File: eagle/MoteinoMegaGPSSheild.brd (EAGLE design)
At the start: 100 x 80 mm, 10 parts, among them Q2 NDP6020P P-CHANNEL

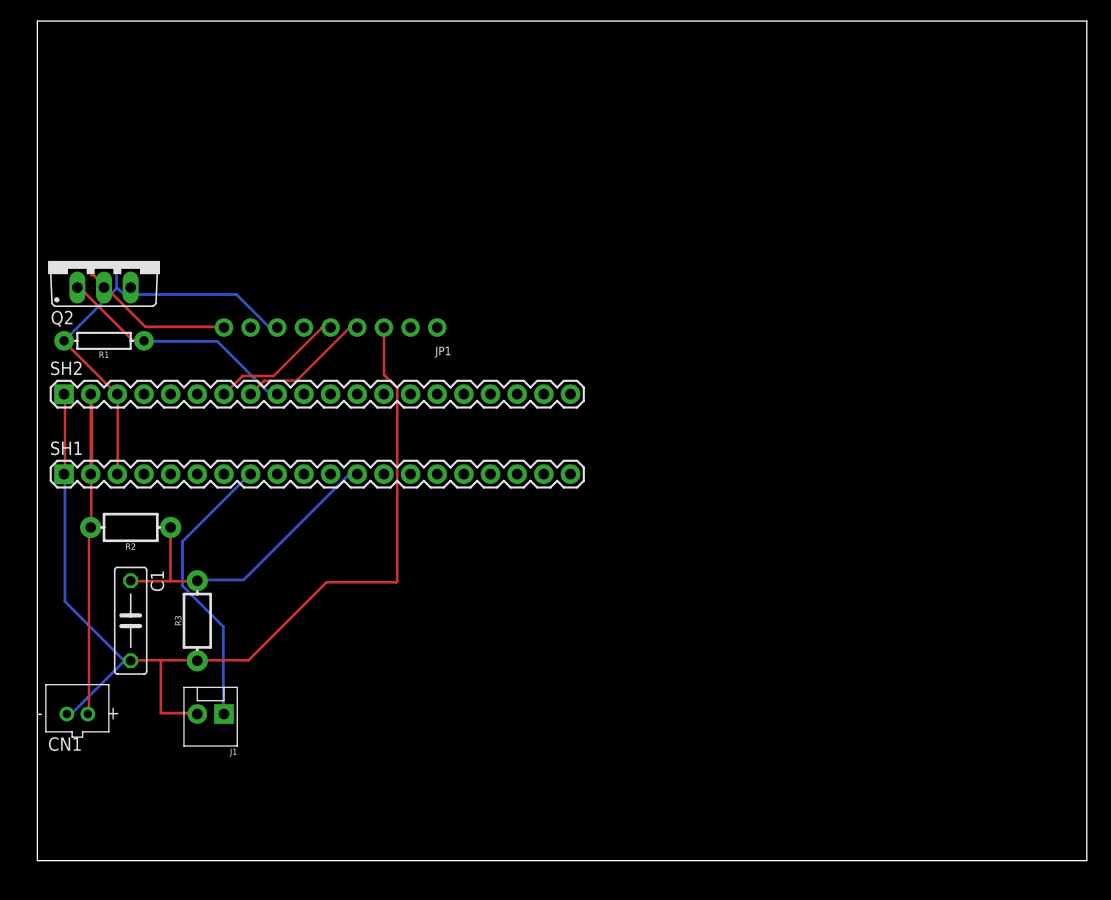
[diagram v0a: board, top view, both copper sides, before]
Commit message: V0.2 No errors, Bottom layer copper pour
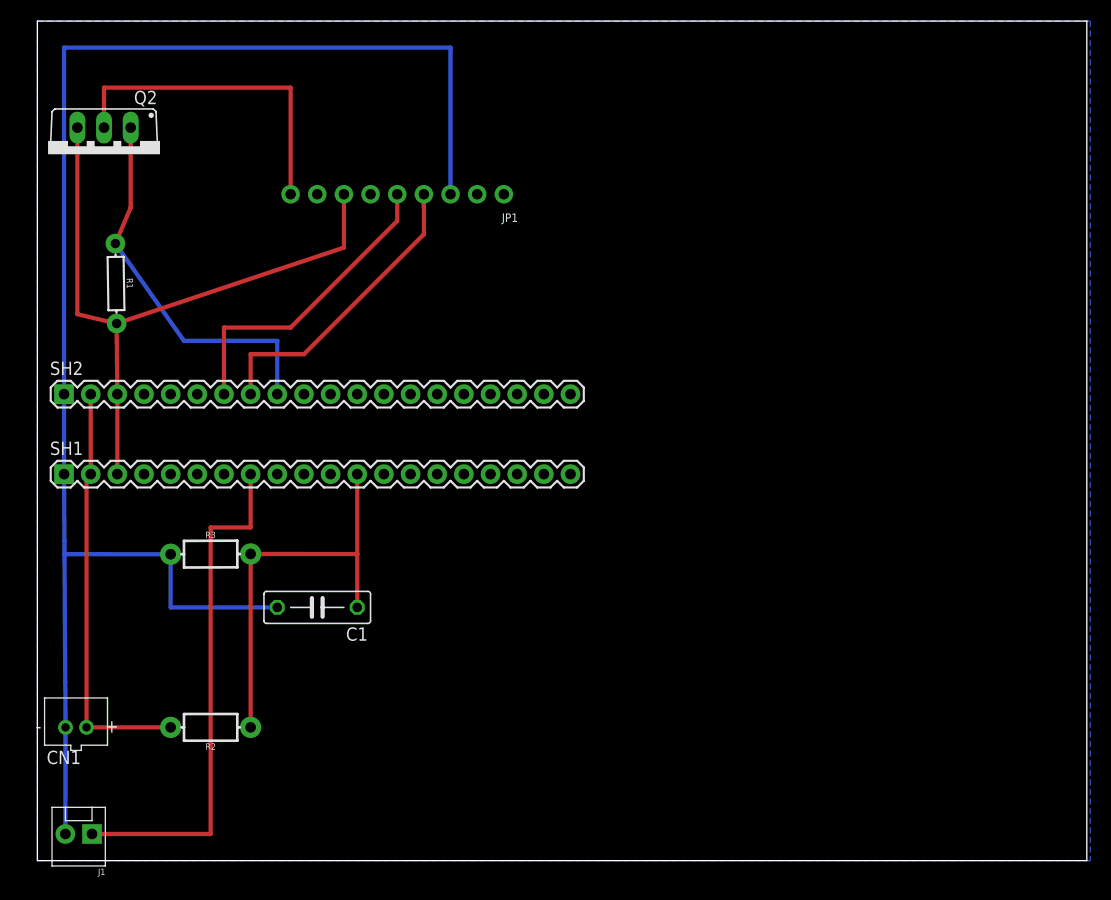
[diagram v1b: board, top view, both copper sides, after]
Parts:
- CN1: value (none) -> JST
- J1: value (none) -> SCREW_TERM
- JP1: value (none) -> GPS_HEADR
- moved R2 20.5 mm to (16.5, 12.7)
- moved C1 17.8 mm to (26.7, 24.1), turned to 180 degrees
- moved J1 17.0 mm to (5.21, 2.54)
- moved JP1 14.2 mm to (34.3, 63.5)
- moved Q2 10.2 mm to (6.35, 67.3), turned to 180 degrees
- moved R3 6.48 mm to (16.5, 29.2), turned to 0.2 degrees
- moved R1 5.58 mm to (7.49, 55.0), turned to 270.9 degrees
- moved CN1 1.28 mm to (3.68, 12.7)
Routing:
- net GND: track 98.5 -> 151.1 mm
- net VBAT: track 40.8 -> 63.9 mm
- net D3: track 27.2 -> 49.4 mm
- net D11_TX1: track 12.8 -> 30.1 mm
- net 3.3V: track 14.8 -> 31.8 mm
- net D10_RX1: track 12.8 -> 29.6 mm
- net D12: track 23.3 -> 36.7 mm
- net PWR: track 30.9 -> 39.9 mm
- net A0: track 30.9 -> 39.4 mm
- added copper zone on layer 16, net GND

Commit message: v0.3 ... GSM plus right Mega headers
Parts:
- removed SH1, SH2: M20, SparkFun-Connectors:1X20
- added FONA_GSM: HEADER, adafruit2:1X12-CB
- added J2, J3, J4, J5, J6: SCREW_TERM, SparkFun-Connectors:SCREWTERMINAL-3.5MM-2-NS
- added U$1: MOTEINO_MEGA_SIMPLE, Moteino:MOTEINO_MEGA_SIMPLE
- C1: value 0.01uF -> 0.1uF
- J1: device SparkFun-Retired:MOLEX-1X2 -> SparkFun-Connectors:SCREWTERMINAL-3.5MM-2-NS
- moved JP1 9.25 mm to (31.8, 72.4)
- moved Q2 8.89 mm to (6.35, 76.2), turned to 0 degrees
- moved R3 7.62 mm to (16.5, 21.6), turned to 0 degrees
- moved R1 7.24 mm to (7.62, 62.2), turned to 0 degrees
- moved C1 6.84 mm to (24.1, 17.8), turned to 0 degrees
- moved CN1 5.08 mm to (3.81, 17.8)
- moved J1 2.95 mm to (2.54, 3.81), turned to 0 degrees
- moved R2 1.27 mm to (16.5, 14.0)
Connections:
- removed net A5: SH1.17
- removed net A6: SH1.18
- removed net A7: SH1.19
- removed net AREF: SH1.20
- removed net D0: SH1.11
- removed net D13: SH2.10
- removed net D14: SH2.11
- removed net D15: SH2.12
- removed net D16: SH2.13
- removed net D17: SH2.14
- removed net D18: SH2.15
- removed net D19: SH2.16
- removed net D2: SH1.9
- removed net D20: SH2.17
- removed net D21: SH2.18
- removed net D22: SH2.19
- removed net D23: SH2.20
- removed net D4_SS: SH1.7
- removed net D5_MOSI: SH1.6
- removed net D6_MISO: SH1.5
- removed net D7_SCK: SH1.4
- removed net PWR: CN1.1, R2.P$2, SH1.2, SH2.2
- removed net RST: SH2.4
- removed net VBAT: JP1.7, Q2.S, R1.P$2, SH1.3, SH2.3
- new net D13_NETSTAT: FONA_GSM.2, U$1.D13
- new net D14_KEY: FONA_GSM.6, U$1.D14
- new net D18_PS: FONA_GSM.7, U$1.D18
- new net N$3: J6.2
- new net SPEAKER2+: FONA_GSM.10
- new net VIN: CN1.1, FONA_GSM.12, R2.P$2, U$1.VIN
- net 3.3V: now also FONA_GSM.1, JP1.7, Q2.S, R1.P$2, U$1.3V3_2
- net A0: now also U$1.A0; no longer SH1.12
- net A1: now also U$1.A1; no longer SH1.13
- net A2: now also J2.2, J3.2, U$1.A2; no longer SH1.14
- net A3: now also J5.2, U$1.A3; no longer SH1.15
- net A4: now also J6.1, U$1.A4; no longer SH1.16
- net D1: now also J4.2, U$1.D1; no longer SH1.10
- net D10_RX1: now also U$1.D10; no longer SH2.7
- net D11_TX1: now also U$1.D11; no longer SH2.8
- net D12: now also U$1.D12; no longer SH2.9
- net D3: now also J1.2, U$1.D3; no longer J1.1, SH1.8
- net D8: now also FONA_GSM.4, U$1.D8; no longer SH2.5
- net D9: now also FONA_GSM.3, U$1.D9; no longer SH2.6
- net GND: now also FONA_GSM.11, J1.1, J2.1, J3.1, J4.1, J5.1, U$1.GND1, U$1.GND_2; no longer J1.2, SH1.1, SH2.1
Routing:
- net GND: track 151.1 -> 0.00 mm
- net 3.3V: track 31.8 -> 127.1 mm
- net VIN: track 0.00 -> 84.4 mm
- net VBAT: track 63.9 -> 0.00 mm
- net D8: track 0.00 -> 50.8 mm
- net D9: track 0.00 -> 45.7 mm
- net D14_KEY: track 0.00 -> 40.6 mm
- net PWR: track 39.9 -> 0.00 mm
- net A1: track 0.00 -> 38.0 mm
- net D1: track 0.00 -> 37.4 mm
- net A2: track 0.00 -> 34.5 mm
- net D18_PS: track 0.00 -> 33.0 mm
- net D13_NETSTAT: track 0.00 -> 33.0 mm
- net A3: track 0.00 -> 29.2 mm
- net A4: track 0.00 -> 26.5 mm
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
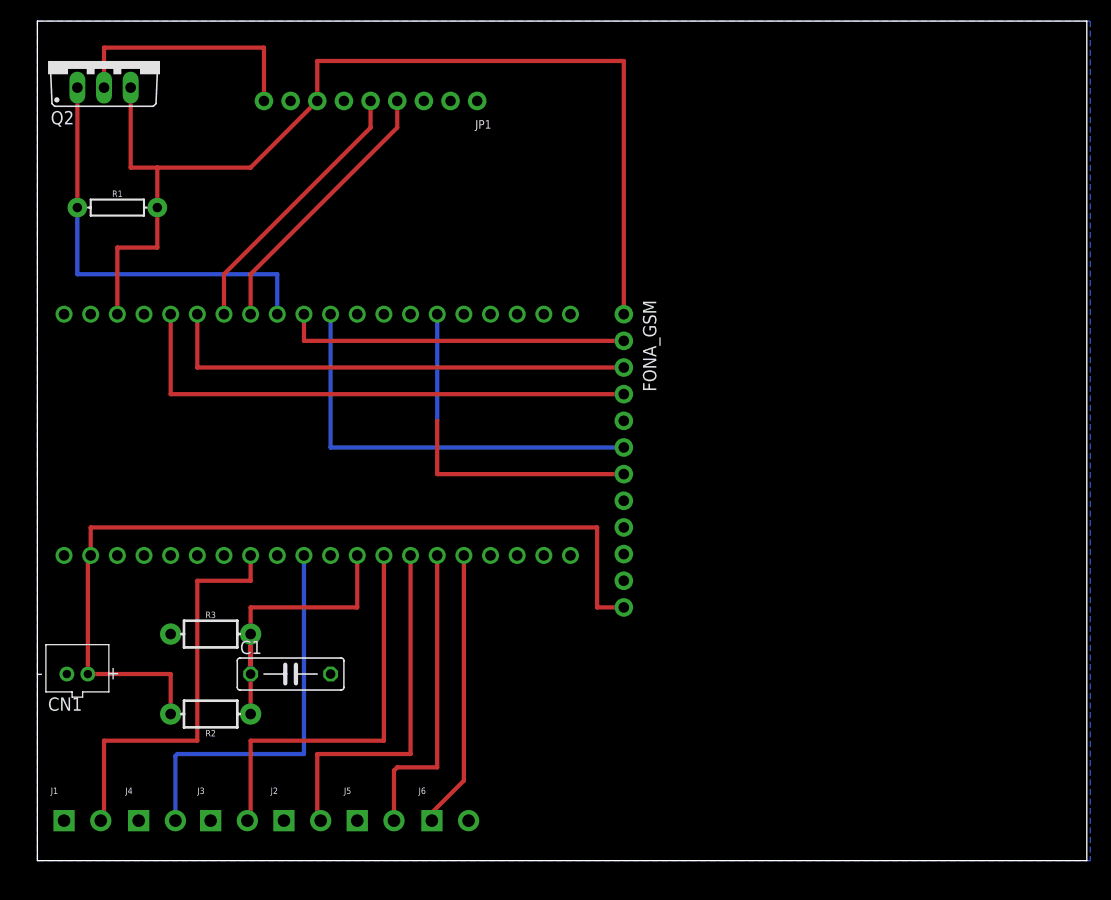
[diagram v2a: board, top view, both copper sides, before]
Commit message: Removing PDFs
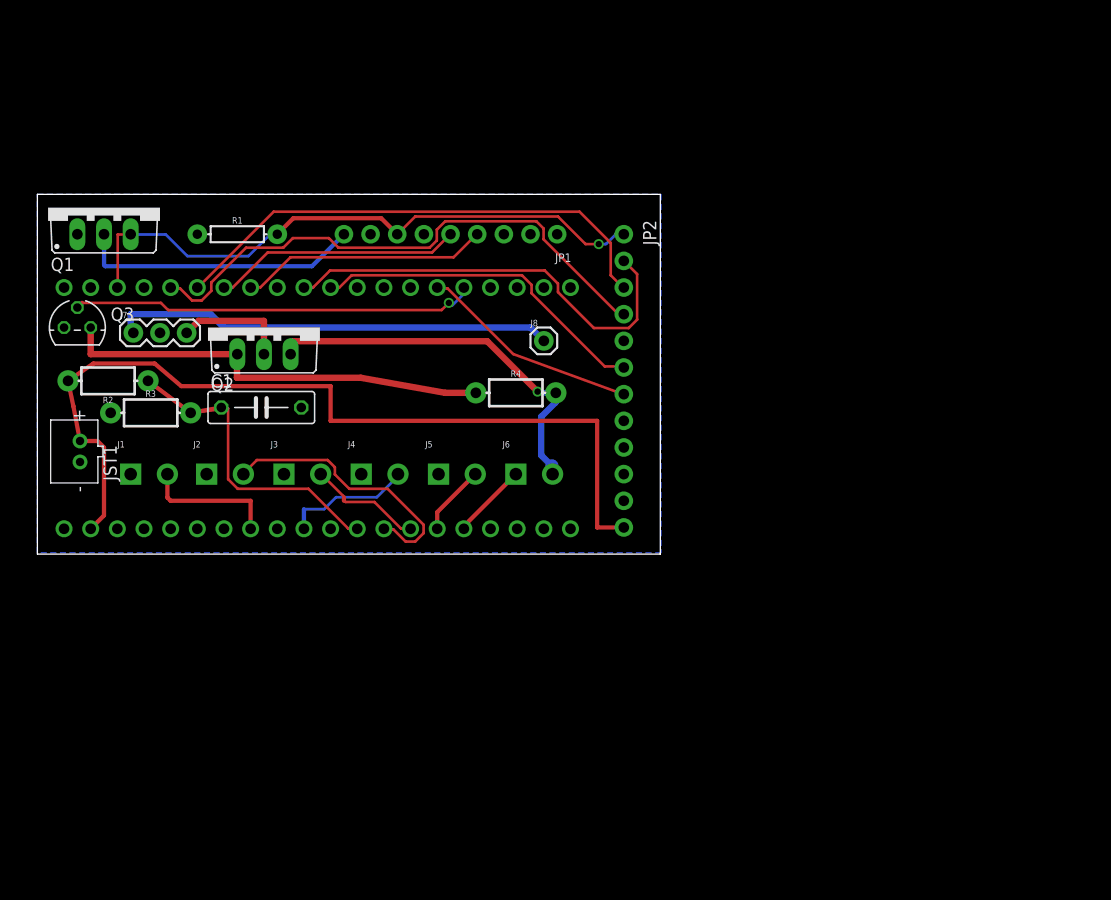
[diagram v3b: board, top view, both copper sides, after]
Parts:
- removed CN1: JST, adafruit:JST-PH-2-THM
- removed FONA_GSM: HEADER, adafruit2:1X12-CB
- removed U$1: MOTEINO_MEGA_SIMPLE, Moteino:MOTEINO_MEGA_SIMPLE
- added J7: OKI-78SR-5/1.5, SparkFun-Connectors:1X03
- added J8: 5V, SparkFun-Connectors:1X01
- added JP2: FONA_GSM, adafruit2:1X12-CB
- added JST1: LIPO, adafruit:JST-PH-2-THM
- added MOTEINO_MEGA: HEADERS, Moteino:MOTEINO_MEGA_SIMPLE
- added Q1: NDP6020P P-CHANNEL, transistor-power:TO220BV
- added Q3: 2N7000, transistors:TO-92
- added R4: 10K, SparkFun-Resistors:AXIAL-0.3-KIT
- J1: value SCREW_TERM -> BilgeSwitch
- J2: value SCREW_TERM -> Button
- J3: value SCREW_TERM -> LED
- J5: value SCREW_TERM -> DS18B20
- J6: value SCREW_TERM -> DS18B20_12-24V_VCC
- Q2: value NDP6020P P-CHANNEL -> IRF9Z14PBF
- moved J4 39.2 mm to (30.9, 36.8)
- moved J6 34.0 mm to (45.6, 36.8)
- moved J5 33.9 mm to (38.2, 36.8)
- moved J2 33.8 mm to (16.1, 36.8)
- moved J3 33.8 mm to (23.5, 36.8)
- moved J1 33.6 mm to (8.89, 36.8)
- moved R2 33.2 mm to (6.73, 45.7)
- moved Q2 29.6 mm to (21.6, 50.8)
- moved C1 25.6 mm to (21.3, 43.2)
- moved R3 21.8 mm to (10.8, 42.7)
- moved JP1 14.8 mm to (39.4, 59.7)
- moved R1 11.7 mm to (19.1, 59.7)
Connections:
- removed net A1: U$1.A1
- removed net A2: J2.2, J3.2, U$1.A2
- removed net A3: J5.2, U$1.A3
- removed net A4: J6.1, U$1.A4
- removed net N$3: J6.2
- new net 12-24V-SW: J7.3, Q2.D
- new net 12-24V-VCC: J6.2, Q2.S, R4.P$2
- new net 5V_VCC: J7.1, J8.1
- new net D19_PWRON: MOTEINO_MEGA.D19, Q3.2
- new net D25: J2.2, MOTEINO_MEGA.A1
- new net D26: J3.2, MOTEINO_MEGA.A2
- new net D27: J5.2, MOTEINO_MEGA.A3
- new net D28: J6.1, MOTEINO_MEGA.A4
- new net GPS_VCC: JP1.9, Q1.D
- new net N$2: Q2.G, Q3.3, R4.P$1
- net 3.3V: now also JP2.1, MOTEINO_MEGA.3V3_2, Q1.S; no longer FONA_GSM.1, JP1.9, Q2.D, Q2.S, U$1.3V3_2
- net A0: now also MOTEINO_MEGA.A0; no longer U$1.A0
- net D1: now also MOTEINO_MEGA.D1; no longer U$1.D1
- net D10_RX1: now also MOTEINO_MEGA.D10; no longer U$1.D10
- net D11_TX1: now also MOTEINO_MEGA.D11; no longer U$1.D11
- net D12: now also MOTEINO_MEGA.D12, Q1.G; no longer Q2.G, U$1.D12
- net D13_NETSTAT: now also JP2.2, MOTEINO_MEGA.D13; no longer FONA_GSM.2, U$1.D13
- net D14_KEY: now also JP2.6, MOTEINO_MEGA.D14; no longer FONA_GSM.6, U$1.D14
- net D18_PS: now also JP2.7, MOTEINO_MEGA.D18; no longer FONA_GSM.7, U$1.D18
- net D3: now also MOTEINO_MEGA.D3; no longer U$1.D3
- net D8: now also JP2.4, MOTEINO_MEGA.D8; no longer FONA_GSM.4, U$1.D8
- net D9: now also JP2.3, MOTEINO_MEGA.D9; no longer FONA_GSM.3, U$1.D9
- net GND: now also J7.2, JP2.11, JST1.2, MOTEINO_MEGA.GND1, MOTEINO_MEGA.GND_2, Q3.1; no longer CN1.2, FONA_GSM.11, U$1.GND1, U$1.GND_2
- net SPEAKER2+: now also JP2.10; no longer FONA_GSM.10
- net VIN: now also JP2.12, JST1.1, MOTEINO_MEGA.VIN; no longer CN1.1, FONA_GSM.12, U$1.VIN
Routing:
- net 3.3V: track 127.1 -> 58.4 mm, vias 0 -> 1
- net 5V_VCC: track 0.00 -> 42.3 mm
- net N$2: track 0.00 -> 41.7 mm
- net D12: track 40.6 -> 0.00 mm
- net D19_PWRON: track 0.00 -> 38.7 mm, vias 0 -> 1
- net A1: track 38.0 -> 0.00 mm
- net 12-24V-VCC: track 0.00 -> 37.2 mm, vias 0 -> 1
- net A2: track 34.5 -> 0.00 mm
- net A3: track 29.2 -> 0.00 mm
- net GPS_VCC: track 0.00 -> 27.1 mm
- net D3: track 39.6 -> 13.0 mm
- net A4: track 26.5 -> 0.00 mm
- net D25: track 0.00 -> 26.2 mm
- net D1: track 37.4 -> 12.3 mm
- net D18_PS: track 33.0 -> 21.1 mm
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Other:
- board size 100 x 80 mm -> 59.4 x 34.3 mm

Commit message: fixes....
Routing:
- net D12: track 0.00 -> 35.5 mm
- net 3.3V: track 58.4 -> 57.8 mm
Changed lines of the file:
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@@
 <attribute name="PROD_ID" value="RES-09559" x="45.593" y="44.577" size="1.778" layer="27" display="off"/>
 </element>
-<element name="Q3" library="transistors" package="TO-92" value="2N7000" x="3.81" y="50.8"/>
+<element name="Q3" library="transistors" package="TO-92" value="2N7000" x="3.81" y="50.8" smashed="yes">
+<attribute name="NAME" x="6.985" y="51.435" size="1.27" layer="25" ratio="10"/>
+<attribute name="VALUE" x="1.143" y="47.752" size="1.27" layer="27" ratio="10"/>
+</element>
 <element name="J7" library="SparkFun-Connectors" package="1X03" value="OKI-78SR-5/1.5" x="9.144" y="50.292">
 <attribute name="PROD_ID" value="XXX-00000" x="9.144" y="50.292" size="1.778" layer="27" display="off"/>
@@
 <contactref element="R1" pad="P$1"/>
 <contactref element="Q1" pad="G"/>
-<wire x1="15.24" y1="59.69" x2="22.86" y2="54.61" width="0" layer="19" extent="1-1"/>
-<wire x1="3.81" y1="59.69" x2="15.24" y2="59.69" width="0" layer="19" extent="1-1"/>
+<wire x1="3.81" y1="59.69" x2="3.81" y2="62.23" width="0.6096" layer="1"/>
+<wire x1="3.81" y1="62.23" x2="11.43" y2="62.23" width="0.6096" layer="1"/>
+<wire x1="11.43" y1="62.23" x2="15.24" y2="59.69" width="0.6096" layer="1"/>
+<wire x1="22.86" y1="54.61" x2="21.717" y2="53.467" width="0.254" layer="1"/>
+<wire x1="21.717" y1="53.467" x2="16.51" y2="53.467" width="0.254" layer="1"/>
+<wire x1="16.51" y1="53.467" x2="16.002" y2="52.959" width="0.254" layer="1"/>
+<wire x1="16.002" y1="52.959" x2="12.446" y2="52.959" width="0.254" layer="1"/>
+<wire x1="12.446" y1="52.959" x2="11.43" y2="53.975" width="0.254" layer="1"/>
+<wire x1="11.43" y1="53.975" x2="11.43" y2="62.23" width="0.254" layer="1"/>
 </signal>
 <signal name="D11_TX1">
@@
 <contactref element="Q1" pad="S"/>
 <contactref element="JP2" pad="1"/>
-<wire x1="8.8011" y1="59.6646" x2="7.6581" y2="59.6646" width="0.254" layer="1"/>
-<wire x1="8.8011" y1="59.6646" x2="8.89" y2="59.69" width="0.254" layer="1"/>
-<wire x1="7.6581" y1="59.6646" x2="7.6581" y2="54.6354" width="0.254" layer="1"/>
 <wire x1="55.0926" y1="59.6646" x2="55.7784" y2="59.6646" width="0.254" layer="16"/>
 <wire x1="54.1782" y1="58.7502" x2="55.0926" y2="59.6646" width="0.254" layer="16"/>
@@
 <wire x1="24.384" y1="61.214" x2="22.86" y2="59.69" width="0.4064" layer="1"/>
 <contactref element="MOTEINO_MEGA" pad="3V3_2"/>
-<wire x1="7.62" y1="54.61" x2="7.6581" y2="54.6354" width="0" layer="19" extent="1-1"/>
+<wire x1="7.62" y1="54.61" x2="7.62" y2="58.42" width="0.4064" layer="1"/>
+<wire x1="7.62" y1="58.42" x2="8.89" y2="59.69" width="0.4064" layer="1"/>
 </signal>
 <signal name="SPEAKER2+">
@@
 <contactref element="MOTEINO_MEGA" pad="D19"/>
 <contactref element="Q3" pad="2"/>
-<wire x1="12.4587" y1="52.4637" x2="11.7729" y2="53.1495" width="0.254" layer="1"/>
-<wire x1="38.5191" y1="52.4637" x2="12.4587" y2="52.4637" width="0.254" layer="1"/>
+<wire x1="9.9187" y1="52.4637" x2="9.2329" y2="53.1495" width="0.254" layer="1"/>
+<wire x1="38.5191" y1="52.4637" x2="9.9187" y2="52.4637" width="0.254" layer="1"/>
 <wire x1="39.2049" y1="53.1495" x2="38.5191" y2="52.4637" width="0.254" layer="1"/>
 <wire x1="39.4335" y1="52.9209" x2="39.2049" y2="53.1495" width="0.254" layer="16"/>
@@
 <wire x1="40.5765" y1="54.5211" x2="40.64" y2="54.61" width="0.254" layer="16"/>
 <via x="39.2049" y="53.1495" extent="1-16" drill="0.6096"/>
-<wire x1="11.7729" y1="53.1495" x2="4.2545" y2="53.1495" width="0.254" layer="1"/>
+<wire x1="9.2329" y1="53.1495" x2="4.2545" y2="53.1495" width="0.254" layer="1"/>
 <wire x1="4.2545" y1="53.1495" x2="3.81" y2="52.705" width="0.4064" layer="1"/>
 </signal>

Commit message: Update
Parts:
- removed J6: DS18B20_12-24V_VCC, SparkFun-Connectors:SCREWTERMINAL-3.5MM-2-NS
- added R5: 27M, SparkFun-Resistors:AXIAL-0.3-KIT
- added R6: 3.3M, SparkFun-Resistors:AXIAL-0.3-KIT
- J4: value SCREW_TERM -> DS18B20
- J5: value DS18B20 -> DS18B20_12-24V_VCC
- moved R4 11.4 mm to (34.2, 44.6)
- moved R3 5.26 mm to (5.59, 41.9)
- moved C1 4.85 mm to (16.5, 42.7)
- moved JST1 2.54 mm to (4.06, 36.4)
- moved R2 1.27 mm to (5.46, 45.7)
- moved J7 0.65 mm to (8.51, 50.4)
- moved Q2 0.51 mm to (21.1, 50.8)
- moved J5 0.25 mm to (38.0, 36.8)
- moved J4 0.13 mm to (30.7, 36.8)
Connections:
- removed net D1: J4.2, MOTEINO_MEGA.D1
- new net A5: MOTEINO_MEGA.A5, R5.P$2, R6.P$2
- net 12-24V-VCC: now also J5.2, R5.P$1; no longer J6.2
- net D27: now also J4.2; no longer J5.2
- net D28: now also J5.1; no longer J6.1
- net GND: now also R6.P$1; no longer J5.1
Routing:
- net A5: track 0.00 -> 47.3 mm
- net 12-24V-VCC: track 37.2 -> 24.5 mm, vias 1 -> 0
- net D1: track 12.3 -> 0.00 mm
- net N$2: track 41.7 -> 31.0 mm
- net D25: track 26.2 -> 17.2 mm
- net VIN: track 84.4 -> 78.6 mm
- net A0: track 32.6 -> 35.7 mm
- net D28: track 7.26 -> 5.88 mm
- net D8: track 52.9 -> 54.0 mm
- net D9: track 48.4 -> 49.4 mm
- net 12-24V-SW: track 11.0 -> 10.3 mm
- net D13_NETSTAT: track 41.6 -> 42.3 mm
- net 3.3V: track 57.8 -> 58.3 mm

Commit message: Added v0.61
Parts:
- added J6: 5V_GDN, SparkFun-Connectors:1X01
- added J9: 12-24V_VCC, SparkFun-Connectors:SCREWTERMINAL-3.5MM-2-NS
- added R7: 50, SparkFun-Resistors:AXIAL-0.3-KIT
- J5: value DS18B20_12-24V_VCC -> DS18B20
- moved R5 8.89 mm to (41.9, 48.3)
- moved R4 4.47 mm to (31.6, 48.3)
- moved Q2 3.82 mm to (20.8, 47.0), turned to 90 degrees
- moved C1 1.80 mm to (15.2, 43.9)
- moved J8 1.80 mm to (47.0, 50.8)
- moved J7 1.27 mm to (9.78, 50.4)
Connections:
- new net N$7: J3.2, R7.P$1
- net 12-24V-VCC: now also J9.1; no longer J5.2
- net D26: now also R7.P$2; no longer J3.2
- net GND: now also J6.1, J9.2
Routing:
- net D13_NETSTAT: track 42.3 -> 31.5 mm
- net N$7: track 0.00 -> 8.01 mm
- net A5: track 47.3 -> 39.5 mm
- net 12-24V-VCC: track 24.5 -> 30.5 mm
- net D26: track 10.5 -> 13.5 mm
- net N$2: track 31.0 -> 28.3 mm
- net VIN: track 78.6 -> 81.0 mm
- net A0: track 35.7 -> 34.0 mm
- net 5V_VCC: track 42.3 -> 41.0 mm
- net D18_PS: track 21.1 -> 21.7 mm
- net 12-24V-SW: track 10.3 -> 9.61 mm
- net D10_RX1: track 24.0 -> 24.6 mm
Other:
- board text added: "G"
- board text added: "GND"
